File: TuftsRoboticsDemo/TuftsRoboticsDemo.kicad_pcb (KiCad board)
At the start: 2 copper layers, 27.6 x 27.6 mm, 8 parts, among them J1 Conn_01x06_Pin, U1 VL53L1CXV0FY1

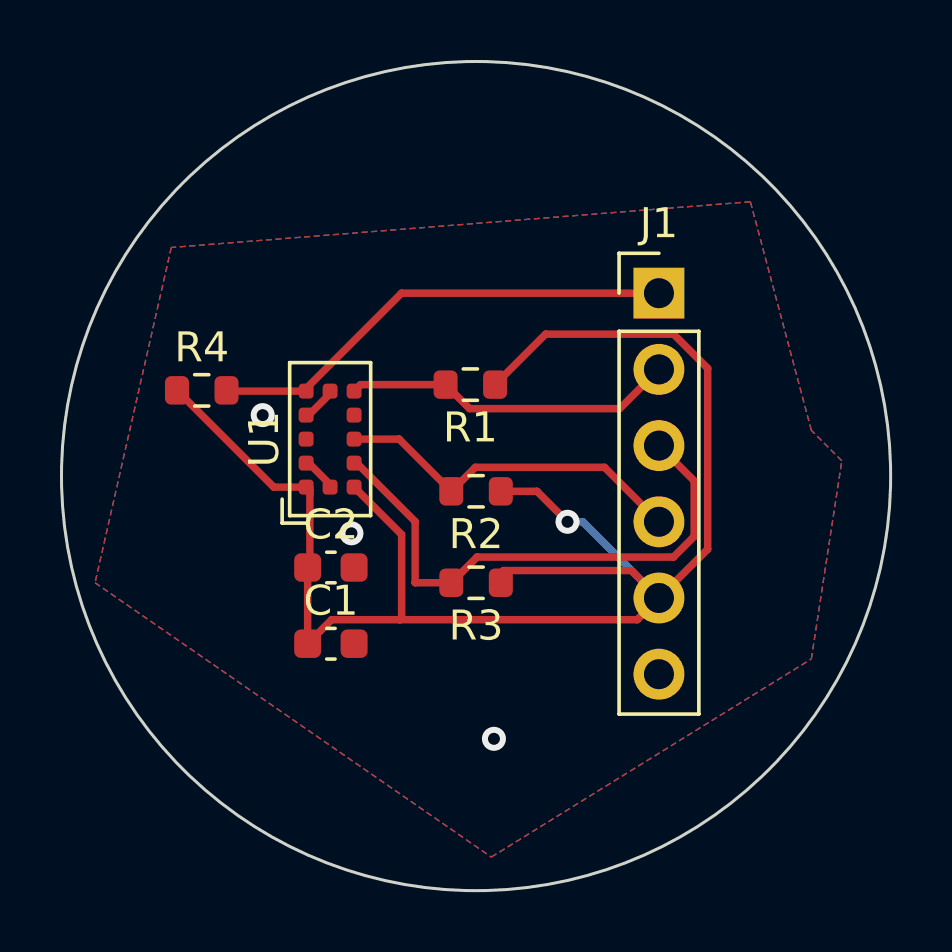
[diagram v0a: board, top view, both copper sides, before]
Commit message: update breakout PCB
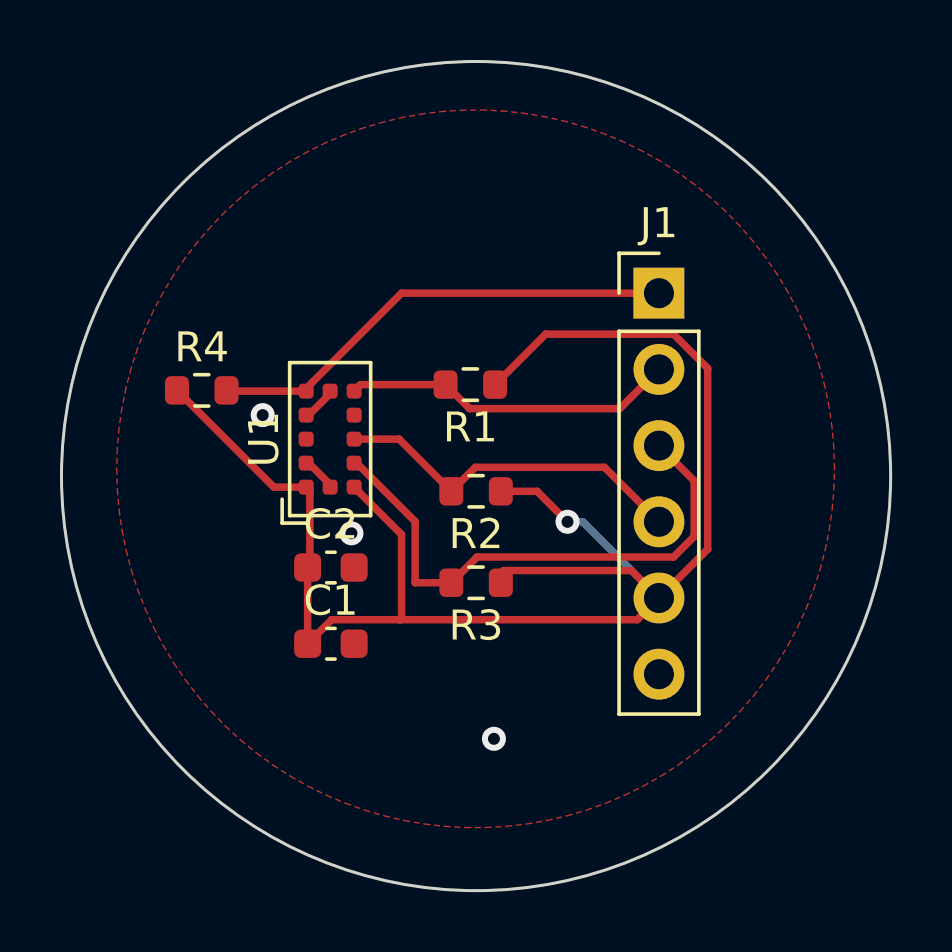
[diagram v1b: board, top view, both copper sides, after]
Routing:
- removed copper zone on B.Cu, net GND
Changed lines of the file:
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@@
   (segment (start 163.284 88.1) (end 165.1 89.916) (width 0.25) (layer "F.Cu") (net 6))
   (segment (start 156.439 87.16) (end 158.179 88.9) (width 0.25) (layer "F.Cu") (net 6))
-  (zone (net 2) (net_name "GND") (layers "F&B.Cu") (hatch edge 0.5)
+  (zone (net 2) (net_name "GND") (layer "F.Cu") (hatch edge 0.5)
     (connect_pads (clearance 0.5))
     (min_thickness 0.25) (filled_areas_thickness no)
@@
     (polygon
       (pts
-        (xy 170.18 86.868)
-        (xy 168.148 79.248)
-        (xy 148.844 80.772)
-        (xy 146.304 91.948)
-        (xy 159.512 101.092)
-        (xy 170.18 94.488)
-        (xy 171.196 87.884)
+        (xy 170.95 88.15)
+        (xy 170.930491 87.467092)
+        (xy 170.872027 86.786412)
+        (xy 170.7748 86.110179)
+        (xy 170.639125 85.4406)
+        (xy 170.465447 84.779859)
+        (xy 170.254331 84.13011)
+        (xy 170.006465 83.493473)
+        (xy 169.722659 82.872025)
+        (xy 169.403839 82.267792)
+        (xy 169.051043 81.682746)
+        (xy 168.665423 81.118795)
+        (xy 168.248237 80.577778)
+        (xy 167.800845 80.061461)
+        (xy 167.324707 79.571526)
+        (xy 166.821375 79.109572)
+        (xy 166.292492 78.677107)
+        (xy 165.739783 78.27554)
+        (xy 165.16505 77.906182)
+        (xy 164.570168 77.570236)
+        (xy 163.957077 77.2688)
+        (xy 163.327778 77.002856)
+        (xy 162.684323 76.773272)
+        (xy 162.028811 76.580796)
+        (xy 161.363379 76.426056)
+        (xy 160.690199 76.309558)
+        (xy 160.011465 76.231681)
+        (xy 159.329393 76.192678)
+        (xy 158.646207 76.192678)
+        (xy 157.964135 76.231681)
+        (xy 157.285401 76.309558)
+        (xy 156.612221 76.426056)
+        (xy 155.946789 76.580796)
+        (xy 155.291277 76.773272)
+        (xy 154.647822 77.002856)
+        (xy 154.018523 77.2688)
+        (xy 153.405432 77.570236)
+        (xy 152.81055 77.906182)
+        (xy 152.235817 78.27554)
+        (xy 151.683108 78.677107)
+        (xy 151.154225 79.109572)
+        (xy 150.650893 79.571526)
+        (xy 150.174755 80.061461)
+        (xy 149.727363 80.577778)
+        (xy 149.310177 81.118795)
+        (xy 148.924557 81.682746)
+        (xy 148.571761 82.267792)
+        (xy 148.252941 82.872025)
+        (xy 147.969135 83.493473)
+        (xy 147.721269 84.13011)
+        (xy 147.510153 84.779859)
+        (xy 147.336475 85.4406)
+        (xy 147.2008 86.110179)
+        (xy 147.103573 86.786412)
+        (xy 147.045109 87.467092)
+        (xy 147.0256 88.15)
+        (xy 147.045109 88.832908)
+        (xy 147.103573 89.513588)
+        (xy 147.2008 90.189821)
+        (xy 147.336475 90.8594)
+        (xy 147.510153 91.520141)
+        (xy 147.721269 92.16989)
+        (xy 147.969135 92.806527)
+        (xy 148.252941 93.427975)
+        (xy 148.571761 94.032208)
+        (xy 148.924557 94.617254)
+        (xy 149.310177 95.181205)
+        (xy 149.727363 95.722222)
+        (xy 150.174755 96.238539)
+        (xy 150.650893 96.728474)
+        (xy 151.154225 97.190428)
+        (xy 151.683108 97.622893)
+        (xy 152.235817 98.02446)
+        (xy 152.81055 98.393818)
+        (xy 153.405432 98.729764)
+        (xy 154.018523 99.0312)
+        (xy 154.647822 99.297144)
+        (xy 155.291277 99.526728)
+        (xy 155.946789 99.719204)
+        (xy 156.612221 99.873944)
+        (xy 157.285401 99.990442)
+        (xy 157.964135 100.068319)
+        (xy 158.646207 100.107322)
+        (xy 159.329393 100.107322)
+        (xy 160.011465 100.068319)
+        (xy 160.690199 99.990442)
+        (xy 161.363379 99.873944)
+        (xy 162.028811 99.719204)
+        (xy 162.684323 99.526728)
+        (xy 163.327778 99.297144)
+        (xy 163.957077 99.0312)
+        (xy 164.570168 98.729764)
+        (xy 165.16505 98.393818)
+        (xy 165.739783 98.02446)
+        (xy 166.292492 97.622893)
+        (xy 166.821375 97.190428)
+        (xy 167.324707 96.728474)
+        (xy 167.800845 96.238539)
+        (xy 168.248237 95.722222)
+        (xy 168.665423 95.181205)
+        (xy 169.051043 94.617254)
+        (xy 169.403839 94.032208)
+        (xy 169.722659 93.427975)
+        (xy 170.006465 92.806527)
+        (xy 170.254331 92.16989)
+        (xy 170.465447 91.520141)
+        (xy 170.639125 90.8594)
+        (xy 170.7748 90.189821)
+        (xy 170.872027 89.513588)
+        (xy 170.930491 88.832908)
+        (xy 170.95 88.15)
       )
     )
